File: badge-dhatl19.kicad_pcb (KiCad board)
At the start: 2 copper layers, 86.4 x 72.4 mm, 26 parts, among them U1 ESP32-WROOM-32, U2 CR2013-MI2120

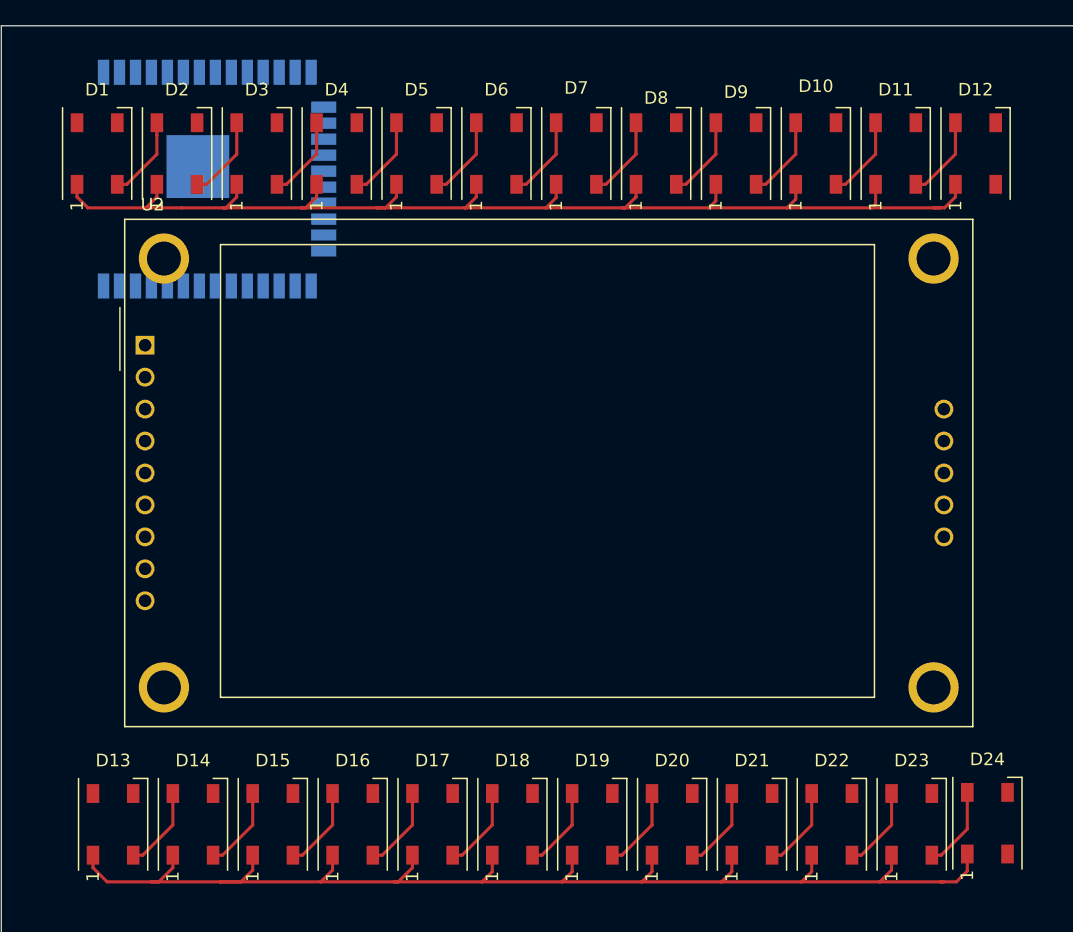
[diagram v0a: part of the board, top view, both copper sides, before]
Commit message: updated led and esp position
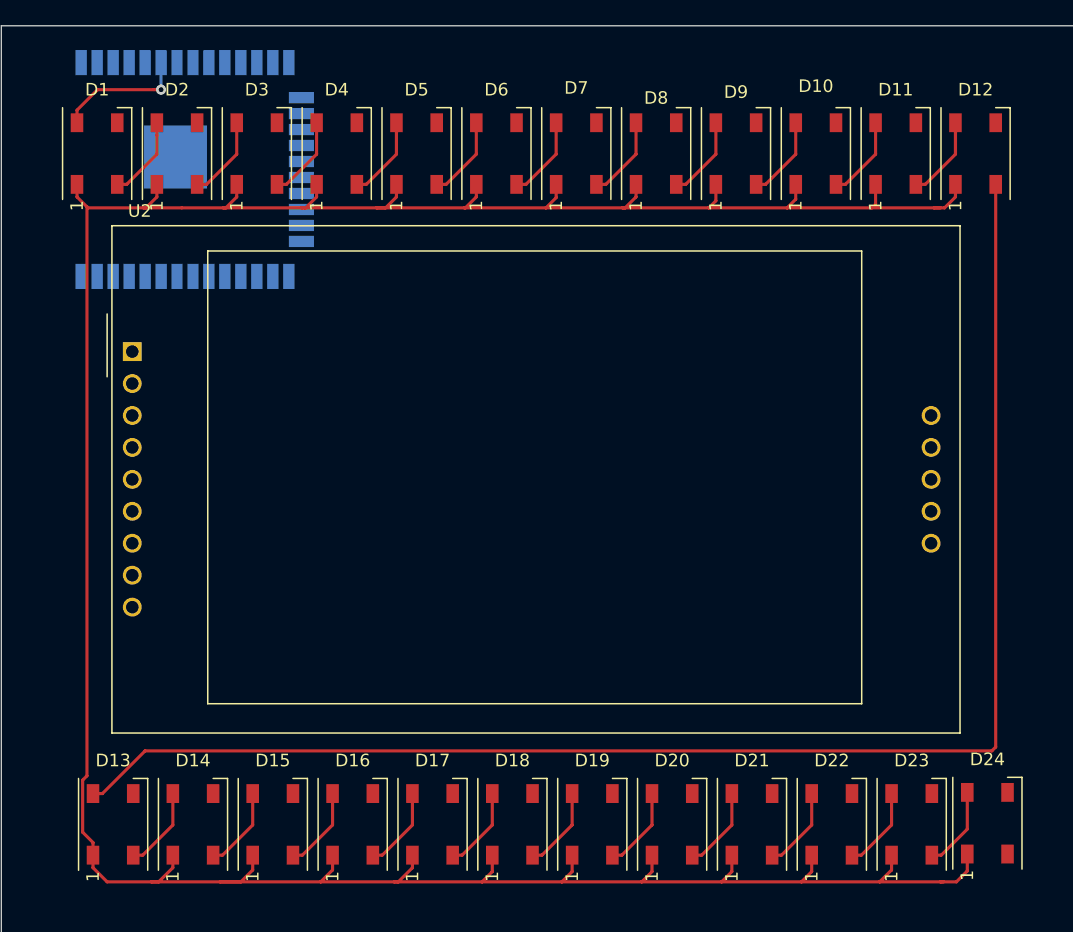
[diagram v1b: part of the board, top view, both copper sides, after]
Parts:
- U2: value CR2013-MI2120 -> ili9341_3.2_touch_sd; footprint Display:CR2013-MI2120 -> Display:ili9341_3.2_touch_sd
- moved U1 1.93 mm to (130.2, 40.6)
- moved U2 1.14 mm to (126.0, 55.1)
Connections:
- net Net-(U2-Pad10) renamed /DISPLAY_T_CLK
- net Net-(U2-Pad11) renamed /DISPLAY_T_CS
- net Net-(U2-Pad12) renamed /DISPLAY_T_DIN
- net Net-(U2-Pad13) renamed /DISPLAY_T_DO
- net Net-(U2-Pad14) renamed /DISPLAY_T_IRQ
- net Net-(U2-Pad8) renamed /DISPLAY_LED
- D1 pad 4: Net-(D1-Pad4) -> /RGB_DIN
- D13 pad 4: Net-(D13-Pad4) -> Net-(D12-Pad2)
- U1 pad 27: Net-(U1-Pad27) -> /DISPLAY_RST
- U1 pad 28: Net-(U1-Pad28) -> /DISPLAY_DC
- U1 pad 29: Net-(U1-Pad29) -> /DISPLAY_CS
- U1 pad 30: Net-(U1-Pad30) -> /DISPLAY_SCK
- U1 pad 31: Net-(U1-Pad31) -> /DISPLAY_MISO
- U1 pad 37: Net-(U1-Pad37) -> /DISPLAY_MOSI
- U1 pad 6: Net-(U1-Pad6) -> /RGB_DIN
- U2 pad 1: Net-(U2-Pad1) -> +3V3
- U2 pad 2: Net-(U2-Pad2) -> GND
- U2 pad 3: Net-(U2-Pad3) -> /DISPLAY_CS
- U2 pad 4: Net-(U2-Pad4) -> /DISPLAY_RST
- U2 pad 5: Net-(U2-Pad5) -> /DISPLAY_DC
- U2 pad 6: Net-(U2-Pad6) -> /DISPLAY_MOSI
- U2 pad 7: Net-(U2-Pad7) -> /DISPLAY_SCK
- U2 pad 9: Net-(U2-Pad9) -> /DISPLAY_MISO
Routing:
- net Net-(D12-Pad2): track 0.00 -> 118.1 mm
- net +5V: track 197.1 -> 249.1 mm
- net /RGB_DIN: track 0.00 -> 10.5 mm, vias 0 -> 1

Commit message: board routing for display nets
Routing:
- net /DISPLAY_MISO: track 0.00 -> 28.7 mm, vias 0 -> 1
- net /DISPLAY_SCK: track 0.00 -> 23.7 mm, vias 0 -> 1
- net /DISPLAY_MOSI: track 0.00 -> 21.5 mm
- net /DISPLAY_DC: track 0.00 -> 20.2 mm, vias 0 -> 1
- net /DISPLAY_RST: track 0.00 -> 18.7 mm, vias 0 -> 1
- net /DISPLAY_CS: track 0.00 -> 15.3 mm, vias 0 -> 1
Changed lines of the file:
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@@
     (thickness 1.6)
     (drawings 5)
-    (tracks 169)
+    (tracks 203)
     (zones 0)
     (modules 26)
@@
   (segment (start 123.22 34.29) (end 127.704315 34.29) (width 0.25) (layer F.Cu) (net 55))
   (segment (start 121.59 36.92) (end 121.59 35.92) (width 0.25) (layer F.Cu) (net 55))
+  (segment (start 123.19 49.14) (end 123.19 67.818) (width 0.25) (layer B.Cu) (net 56))
+  (segment (start 123.19 67.818) (end 123.19 67.818) (width 0.25) (layer B.Cu) (net 56))
+  (segment (start 123.19 67.818) (end 125.984 67.818) (width 0.25) (layer B.Cu) (net 56))
+  (segment (start 130.81 58.293) (end 130.81 58.293) (width 0.25) (layer B.Cu) (net 57))
+  (segment (start 130.81 49.14) (end 130.81 71.374) (width 0.25) (layer B.Cu) (net 57))
+  (segment (start 130.81 71.374) (end 130.81 71.374) (width 0.25) (layer B.Cu) (net 57))
+  (via (at 130.81 71.374) (size 0.8) (drill 0.4) (layers F.Cu B.Cu) (net 57))
+  (segment (start 126.746 75.438) (end 125.984 75.438) (width 0.25) (layer F.Cu) (net 57))
+  (segment (start 130.81 71.374) (end 126.746 75.438) (width 0.25) (layer F.Cu) (net 57))
+  (segment (start 132.08 56.769) (end 132.08 56.769) (width 0.25) (layer B.Cu) (net 58))
+  (segment (start 132.08 49.14) (end 132.08 61.849) (width 0.25) (layer B.Cu) (net 58))
+  (segment (start 132.08 61.849) (end 132.08 61.849) (width 0.25) (layer B.Cu) (net 58))
+  (via (at 132.08 61.849) (size 0.8) (drill 0.4) (layers F.Cu B.Cu) (net 58))
+  (segment (start 132.08 64.262) (end 125.984 70.358) (width 0.25) (layer F.Cu) (net 58))
+  (segment (start 132.08 61.849) (end 132.08 64.262) (width 0.25) (layer F.Cu) (net 58))
+  (segment (start 133.35 49.14) (end 133.35 54.864) (width 0.25) (layer B.Cu) (net 59))
+  (segment (start 133.35 54.864) (end 133.35 54.864) (width 0.25) (layer B.Cu) (net 59))
+  (segment (start 133.35 54.864) (end 133.35 54.864) (width 0.25) (layer B.Cu) (net 59))
+  (via (at 133.35 54.864) (size 0.8) (drill 0.4) (layers F.Cu B.Cu) (net 59))
+  (segment (start 128.016 60.198) (end 125.984 60.198) (width 0.25) (layer F.Cu) (net 59))
+  (segment (start 133.35 54.864) (end 128.016 60.198) (width 0.25) (layer F.Cu) (net 59))
+  (segment (start 134.62 53.086) (end 134.62 53.086) (width 0.25) (layer B.Cu) (net 60))
+  (segment (start 134.62 49.14) (end 134.62 57.404) (width 0.25) (layer B.Cu) (net 60))
+  (segment (start 134.62 57.404) (end 134.62 57.404) (width 0.25) (layer B.Cu) (net 60))
+  (via (at 134.62 57.404) (size 0.8) (drill 0.4) (layers F.Cu B.Cu) (net 60))
+  (segment (start 126.746 65.278) (end 125.984 65.278) (width 0.25) (layer F.Cu) (net 60))
+  (segment (start 134.62 57.404) (end 126.746 65.278) (width 0.25) (layer F.Cu) (net 60))
+  (segment (start 135.89 49.14) (end 135.89 51.689) (width 0.25) (layer B.Cu) (net 61))
+  (segment (start 135.89 51.689) (end 135.89 51.816) (width 0.25) (layer B.Cu) (net 61))
+  (via (at 135.89 51.689) (size 0.8) (drill 0.4) (layers F.Cu B.Cu) (net 61))
+  (segment (start 127.04466 62.738) (end 125.984 62.738) (width 0.25) (layer F.Cu) (net 61))
+  (segment (start 127.438002 62.738) (end 127.04466 62.738) (width 0.25) (layer F.Cu) (net 61))
+  (segment (start 135.89 54.286002) (end 127.438002 62.738) (width 0.25) (layer F.Cu) (net 61))
+  (segment (start 135.89 51.689) (end 135.89 54.286002) (width 0.25) (layer F.Cu) (net 61))
 )

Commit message: added SAO
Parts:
- added X1: Badgelife_sao_connector_v169bis, badgelife_shitty_addon_v169bis:Badgelife-SAOv169-BADGE-2x3, F.Cu at (191.3, 29.2)
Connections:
- U1 pad 11: Net-(U1-Pad11) -> /SAO_GPIO1
- U1 pad 12: Net-(U1-Pad12) -> /SAO_GPIO2
- U1 pad 8: Net-(U1-Pad8) -> /SAO_SCL
- U1 pad 9: Net-(U1-Pad9) -> /SAO_SDA
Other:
- board size 86.4 x 72.4 mm -> 86.4 x 77.5 mm

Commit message: updated schematic and pcb
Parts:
- removed D1, D10, D11, D12, D13, D14, D15, D16, D17, D18, D19, D2, D20, D21, D22, D23, D24, D3, D4, D5, D6, D7, D8, D9: WS2812B, LED_SMD:LED_WS2812B_PLCC4_5.0x5.0mm_P3.2mm
- U1: value ESP32-WROOM-32 -> LolinD32_pro; footprint RF_Module:ESP32-WROOM-32 -> badge-dhatl19:LolinD32_pro; moved to F.Cu
- moved U1 54.2 mm to (76.2, 45.5), turned to 0 degrees
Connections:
- net Net-(U1-Pad18) renamed /RGB_DIN1
- U1 pad 1: GND -> +3V3
- U1 pad 10: Net-(U1-Pad10) -> /DISPLAY_DC
- U1 pad 11: /SAO_GPIO1 -> /DISPLAY_CS
- U1 pad 12: /SAO_GPIO2 -> /SD_CS
- U1 pad 15: GND -> Net-(U1-Pad15)
- U1 pad 17: Net-(U1-Pad17) -> GND
- U1 pad 19: Net-(U1-Pad19) -> /SAO_SDA
- U1 pad 2: +3V3 -> Net-(U1-Pad2)
- U1 pad 20: Net-(U1-Pad20) -> /SAO_GPIO1
- U1 pad 21: Net-(U1-Pad21) -> /SAO_GPIO2
- U1 pad 22: Net-(U1-Pad22) -> /SAO_SCL
- U1 pad 25: Net-(U1-Pad25) -> /DISPLAY_SCK
- U1 pad 26: Net-(U1-Pad26) -> /DISPLAY_MOSI
- U1 pad 27: /DISPLAY_RST -> Net-(U1-Pad27)
- U1 pad 28: /DISPLAY_DC -> Net-(U1-Pad28)
- U1 pad 29: /DISPLAY_CS -> Net-(U1-Pad29)
- U1 pad 30: /DISPLAY_SCK -> Net-(U1-Pad30)
- U1 pad 6: /RGB_DIN -> /DISPLAY_LED
- U1 pad 7: Net-(U1-Pad7) -> /DISPLAY_RST
- U1 pad 8: /SAO_SCL -> Net-(U1-Pad8)
- U1 pad 9: /SAO_SDA -> Net-(U1-Pad9)
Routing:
- net +5V: track 249.1 -> 0.00 mm
- net Net-(D12-Pad2): track 118.1 -> 0.43 mm
- net /DISPLAY_MISO: track 28.7 -> 0.76 mm, vias 1 -> 0
- net /DISPLAY_SCK: track 23.7 -> 0.00 mm, vias 1 -> 0
- net /DISPLAY_MOSI: track 21.5 -> 0.00 mm
- net /DISPLAY_DC: track 20.2 -> 0.00 mm, vias 1 -> 0
- net /DISPLAY_RST: track 18.7 -> 0.00 mm, vias 1 -> 0
- net /DISPLAY_CS: track 15.3 -> 0.00 mm, vias 1 -> 0
- net /RGB_DIN: track 10.5 -> 0.00 mm, vias 1 -> 0
- net Net-(D7-Pad2): track 6.64 -> 0.00 mm
- net Net-(D6-Pad2): track 6.64 -> 0.00 mm
- net Net-(D5-Pad2): track 6.64 -> 0.00 mm
- net Net-(D4-Pad2): track 6.64 -> 0.00 mm
- net Net-(D2-Pad2): track 6.64 -> 0.00 mm
- net Net-(D11-Pad2): track 6.64 -> 0.00 mm
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
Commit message: updated pcb
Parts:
- added D1: ws2812strip12x, badge-dhatl19:ws2812strip12x, F.Cu at (158.8, 38.5)
- added D2: ws2812strip12x, badge-dhatl19:ws2812strip12x, F.Cu at (158.5, 93.5)
- U1: moved to B.Cu
- moved U1 5.95 mm to (72.9, 50.4), turned to 270 degrees

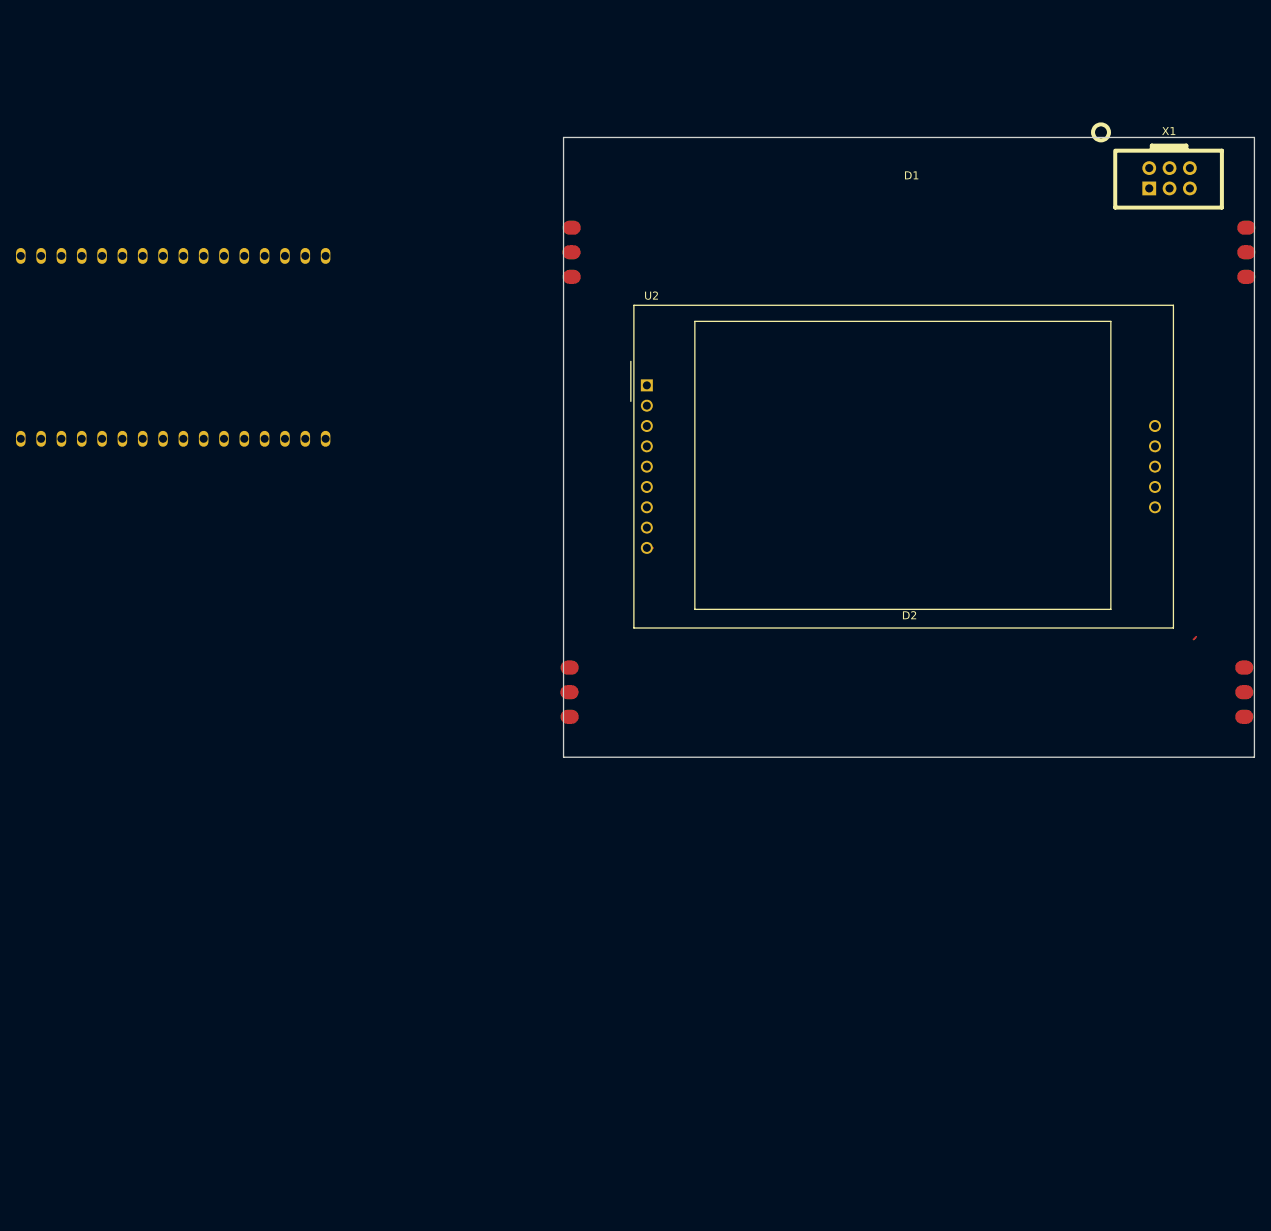
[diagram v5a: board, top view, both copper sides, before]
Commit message: added display footprint and routed board
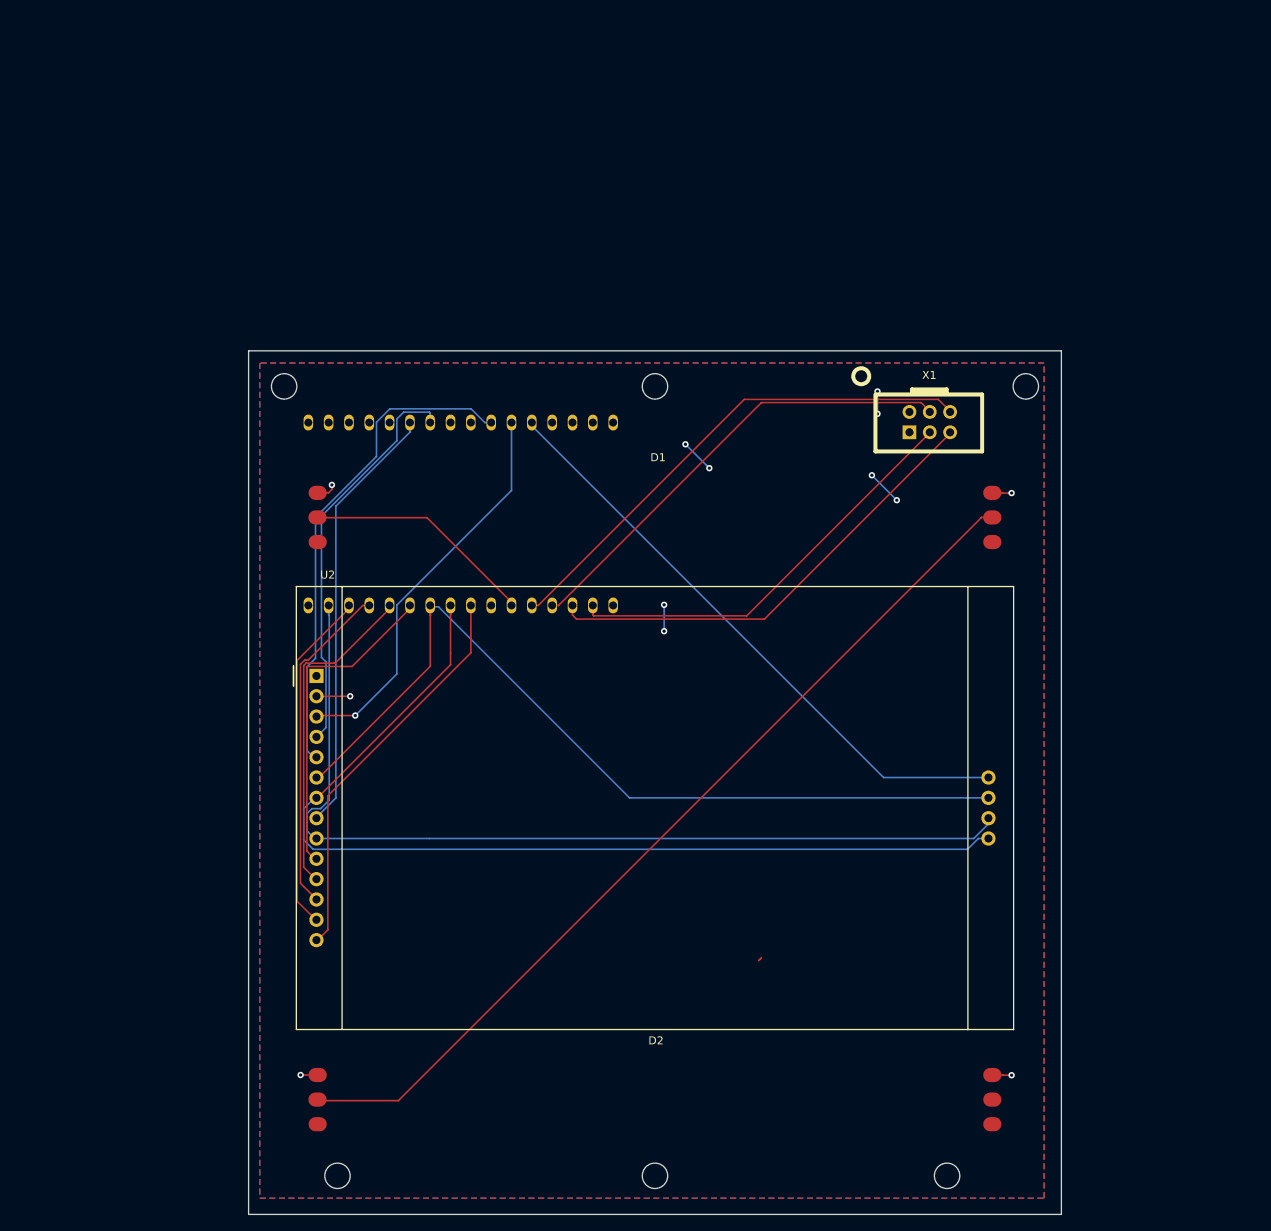
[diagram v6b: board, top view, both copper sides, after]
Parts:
- U2: footprint Display:ili9341_3.2_touch_sd -> badge-dhatl19:ili9341_3.2_touch_sd
- moved D2 59.9 mm to (127.0, 144.4)
- moved U2 52.8 mm to (127.0, 108.0)
- moved D1 45.9 mm to (127.0, 71.6)
- moved X1 42.7 mm to (161.3, 59.7)
- moved U1 41.5 mm to (108.8, 71.2)
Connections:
- D1 pad 1: Net-(D1-Pad1) -> GND
- D1 pad 3: Net-(D1-Pad3) -> +3V3
- D2 pad 1: Net-(D2-Pad1) -> GND
- D2 pad 3: Net-(D2-Pad3) -> +3V3
- U1 pad 18: /RGB_DIN1 -> /SAO_SCL
- U1 pad 19: /SAO_SDA -> /SAO_GPIO2
- U1 pad 20: /SAO_GPIO1 -> /SAO_SDA
- U1 pad 21: /SAO_GPIO2 -> /SAO_GPIO1
- U1 pad 22: /SAO_SCL -> /RGB_DIN1
- U1 pad 24: Net-(U1-Pad24) -> /DISPLAY_T_IRQ
- U1 pad 27: Net-(U1-Pad27) -> /DISPLAY_T_CLK
- U1 pad 28: Net-(U1-Pad28) -> /DISPLAY_T_CS
- U1 pad 29: Net-(U1-Pad29) -> /DISPLAY_T_DIN
- U1 pad 30: Net-(U1-Pad30) -> /DISPLAY_T_DO
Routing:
- net /DISPLAY_SCK: track 0.00 -> 124.3 mm
- net /DISPLAY_MISO: track 0.76 -> 117.0 mm
- net Net-(D1-Pad5): track 0.00 -> 114.5 mm
- net /DISPLAY_MOSI: track 0.00 -> 107.9 mm
- net /SD_CS: track 0.00 -> 75.8 mm
- net /SAO_GPIO1: track 0.00 -> 63.4 mm
- net /DISPLAY_DC: track 0.00 -> 61.6 mm
- net /SAO_GPIO2: track 0.00 -> 58.3 mm
- net /SAO_SDA: track 0.00 -> 57.9 mm
- net /DISPLAY_LED: track 0.00 -> 54.3 mm
- net /SAO_SCL: track 0.00 -> 53.0 mm
- net /DISPLAY_RST: track 0.00 -> 50.3 mm
- net /DISPLAY_T_IRQ: track 0.00 -> 49.9 mm
- net /DISPLAY_CS: track 0.00 -> 49.0 mm, vias 0 -> 1
- net /DISPLAY_T_DO: track 0.00 -> 42.9 mm
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- added copper zone on F.Cu, net +3V3
- added copper zone on B.Cu, net GND
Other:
- board size 86.4 x 77.5 mm -> 101.6 x 108 mm
- rule pad_to_mask_clearance: 0.051 -> 0.0508
- rule solder_mask_min_width: 0.25 -> 0.1016
- rule trace_min: 0.2 -> 0.1524
- rule via_min_size: 0.4 -> 0.508
